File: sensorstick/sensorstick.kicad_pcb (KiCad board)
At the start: 2 copper layers, 85 x 23 mm, 8 parts, among them J1 U217-04XN-XXR84, U1 ESP32-C3_SUPERMINI, U2 SCD40 CO2 module

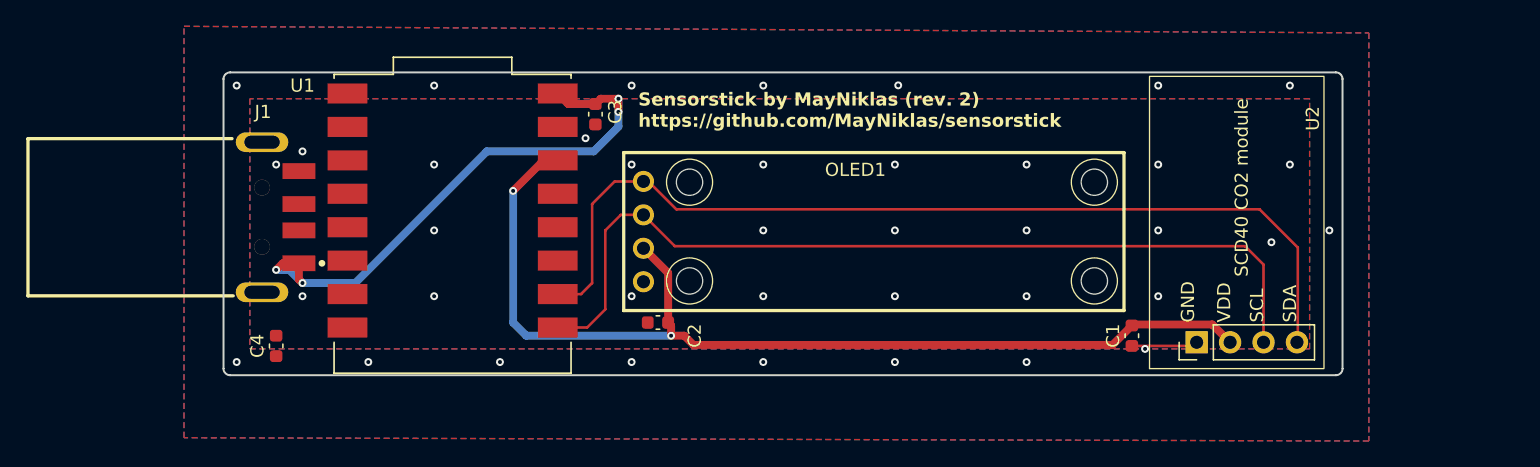
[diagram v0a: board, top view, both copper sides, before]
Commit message: Add RGB LED
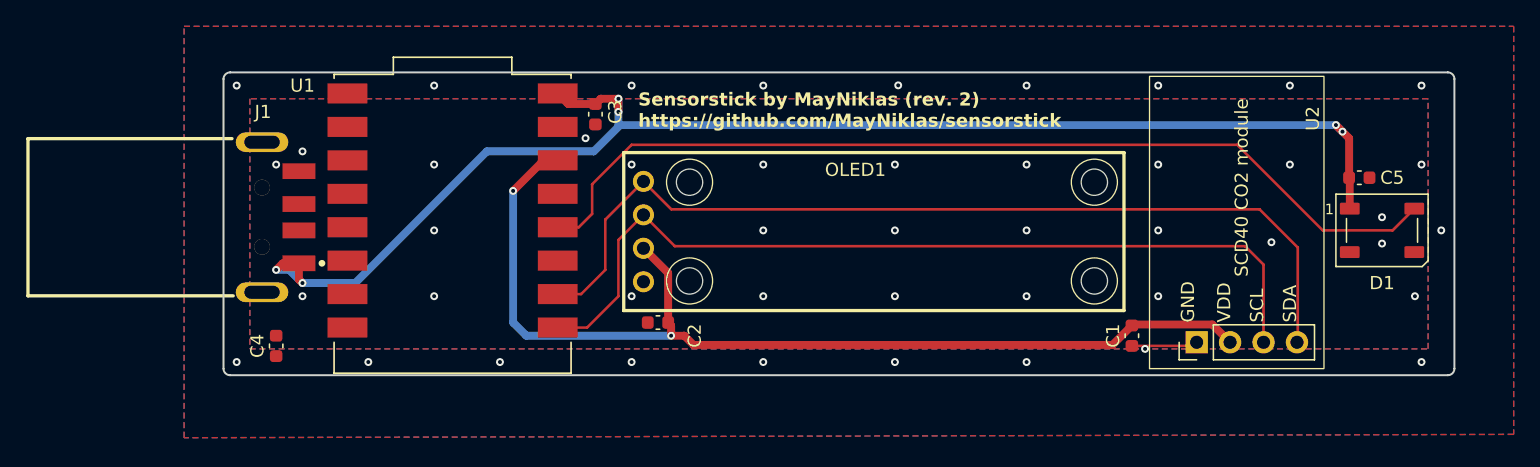
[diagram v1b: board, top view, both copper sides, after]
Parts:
- added C5: 100nF, Capacitor_SMD:C_0603_1608Metric, F.Cu at (146.3, 95.5)
- added D1: WS2812B, LED_SMD:LED_WS2812B_PLCC4_5.0x5.0mm_P3.2mm, F.Cu at (148.0, 99.5)
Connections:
- net /IC2_SDA renamed /I2C_SDA
- U1 pad 3: unconnected-(U1-GPIO3-Pad3) -> /LED_RGB
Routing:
- net /LED_RGB: track 0.00 -> 72.4 mm
- net +5V: track 43.1 -> 105.2 mm, vias 4 -> 6
- net /I2C_SDA: track 72.6 -> 71.3 mm
- net /I2C_SCL: track 68.1 -> 67.1 mm
- net GND: vias 24 -> 28
- net Earth: vias 15 -> 18
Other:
- board size 85 x 23 mm -> 93.5 x 23 mm
